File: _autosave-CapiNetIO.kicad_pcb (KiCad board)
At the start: 2 copper layers, 58 parts, among them J1 USB_B_Micro, J2 SWD Prg, J4 USART3, J5 InterPCBBus1, J6 InterPCBBus2, SW1 SW_SPDT, U1 STM32F446RETx, U2 SN65HVD1781D, U3 AMS1117-3.3, U4 TLP290-4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

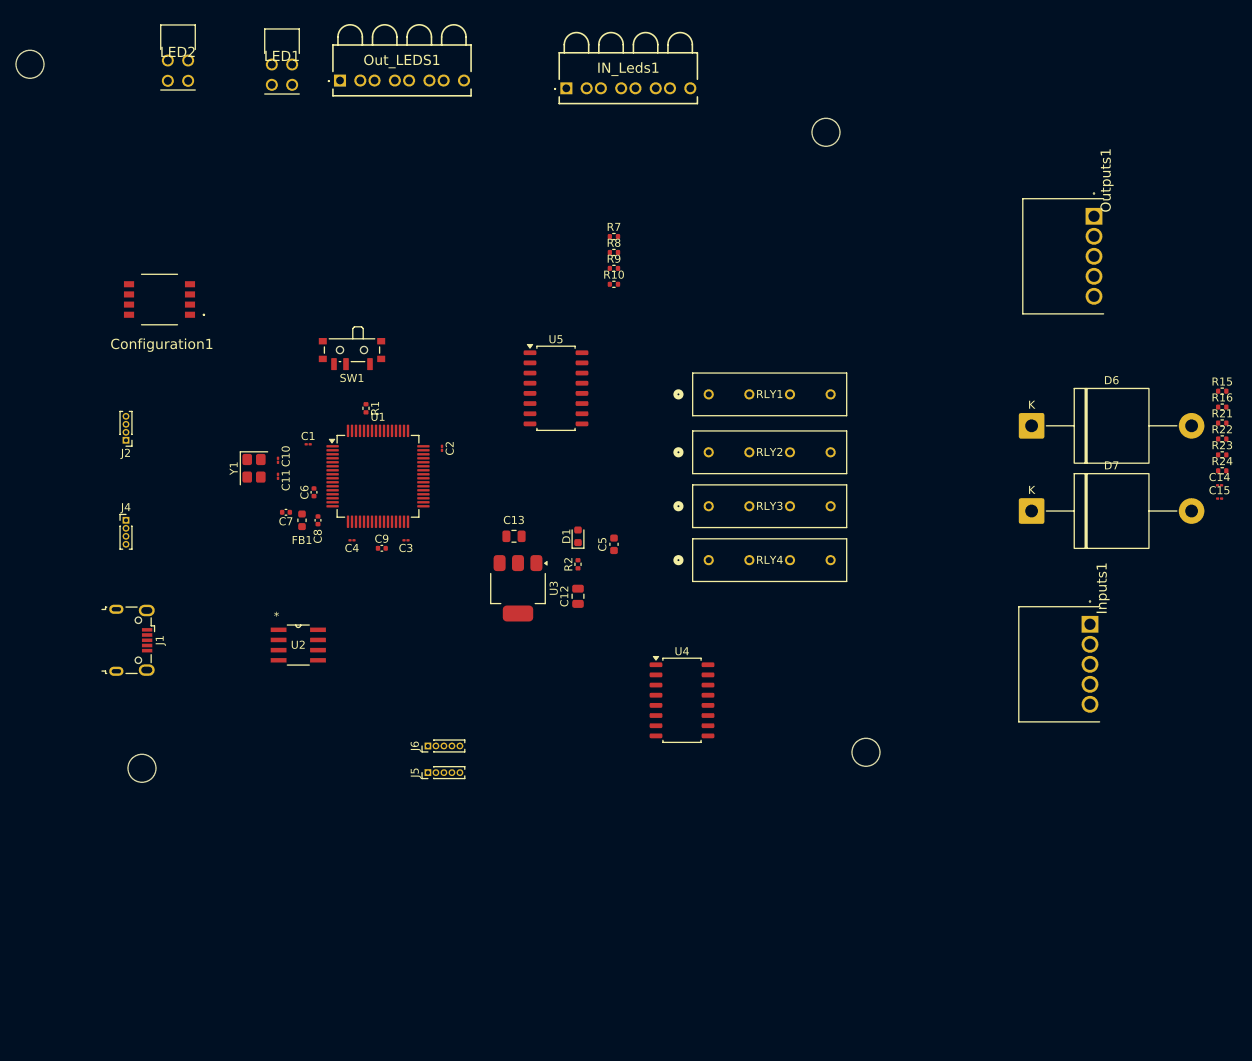
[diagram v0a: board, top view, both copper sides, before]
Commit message: checking components are present in pcb and renaming
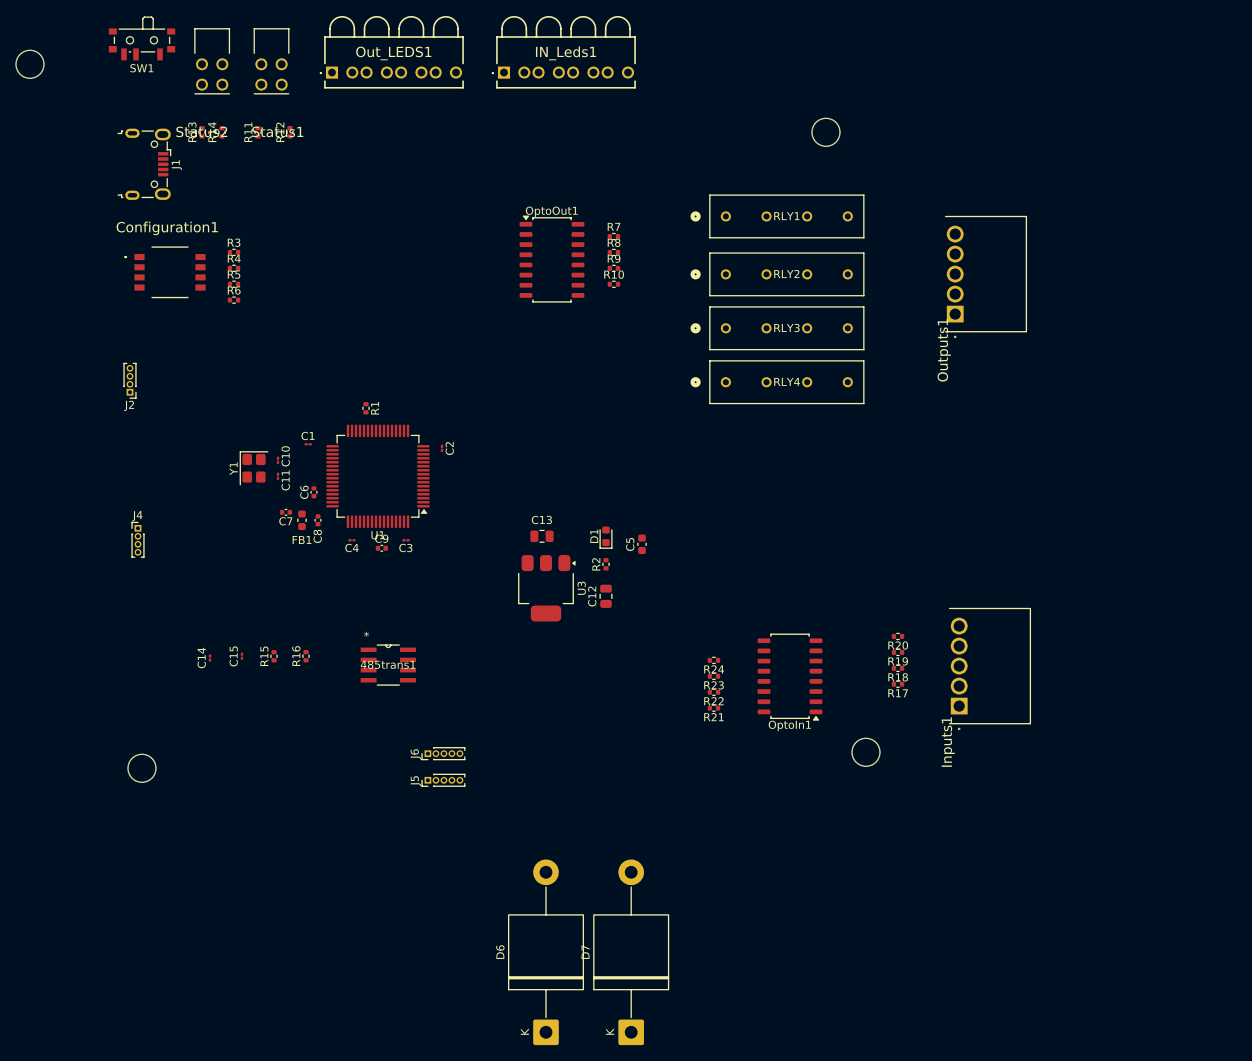
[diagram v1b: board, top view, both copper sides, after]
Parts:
- removed LED1, LED2: 553-0122F, LED 553-0122F:5530122F
- removed U2: SN65HVD1781D, SN65HVD1781D:SN65HVD1781D
- removed U4, U5: TLP290-4, Package_SO:SOP-16_4.55x10.3mm_P1.27mm
- added 485trans1: SN65HVD1781D, SN65HVD1781D:SN65HVD1781D, F.Cu at (87.3, 115.1)
- added OptoIn1: TLP290-4, Package_SO:SOP-16_4.55x10.3mm_P1.27mm, F.Cu at (137.5, 116.5)
- added OptoOut1: TLP290-4, Package_SO:SOP-16_4.55x10.3mm_P1.27mm, F.Cu at (107.8, 64.4)
- added R11: 1k5, Resistor_SMD:R_0402_1005Metric, F.Cu at (71.0, 48.5)
- added R12: 1k5, Resistor_SMD:R_0402_1005Metric, F.Cu at (75.0, 48.5)
- added R13: 1k5, Resistor_SMD:R_0402_1005Metric, F.Cu at (64.0, 48.5)
- added R14: 1k5, Resistor_SMD:R_0402_1005Metric, F.Cu at (66.5, 48.5)
- added R17: 1k, Resistor_SMD:R_0402_1005Metric, F.Cu at (151.0, 117.5)
- added R18: 1k, Resistor_SMD:R_0402_1005Metric, F.Cu at (151.0, 115.5)
- added R19: 1k, Resistor_SMD:R_0402_1005Metric, F.Cu at (151.0, 113.5)
- added R20: 1k, Resistor_SMD:R_0402_1005Metric, F.Cu at (151.0, 111.5)
- added R3: 10K, Resistor_SMD:R_0402_1005Metric, F.Cu at (68.0, 63.5)
- added R4: 10K, Resistor_SMD:R_0402_1005Metric, F.Cu at (68.0, 65.5)
- added R5: 10K, Resistor_SMD:R_0402_1005Metric, F.Cu at (68.0, 67.5)
- added R6: 10K, Resistor_SMD:R_0402_1005Metric, F.Cu at (68.0, 69.5)
- added Status1: 553-0122F, LED 553-0122F:5530122F, F.Cu at (74.0, 40.0)
- added Status2: 553-0122F, LED 553-0122F:5530122F, F.Cu at (66.5, 40.0)
- moved C14 128.0 mm to (65.0, 114.2), turned to 90 degrees
- moved C15 123.8 mm to (69.0, 114.0), turned to 90 degrees
- moved R15 123.1 mm to (73.0, 114.0), turned to 90 degrees
- moved R16 118.7 mm to (77.0, 114.0), turned to 90 degrees
- moved D6 97.1 mm to (107.0, 161.0), turned to 90 degrees
- moved D7 82.2 mm to (117.7, 161.0), turned to 90 degrees
- moved R21 72.9 mm to (128.0, 120.5), turned to 180 degrees
- moved R22 71.0 mm to (128.0, 118.5), turned to 180 degrees
- moved R23 69.3 mm to (128.0, 116.5), turned to 180 degrees
- moved R24 67.8 mm to (128.0, 114.5), turned to 180 degrees
- moved J1 59.5 mm to (57.3, 52.5)
- moved SW1 46.8 mm to (56.5, 37.3)
- moved RLY1 22.3 mm to (129.5, 59.0)
- moved RLY4 22.3 mm to (129.5, 79.7)
- moved RLY2 22.3 mm to (129.5, 66.3)
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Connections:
- net /485A renamed /485A+
- net /485B renamed /485B-
